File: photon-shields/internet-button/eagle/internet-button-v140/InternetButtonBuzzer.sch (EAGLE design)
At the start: 41 parts

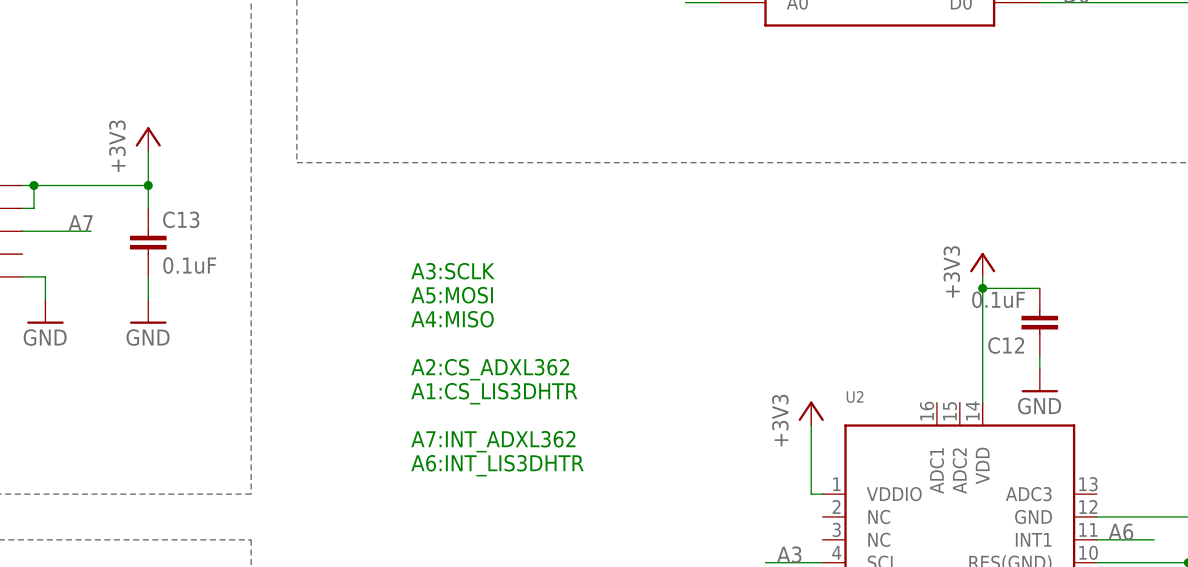
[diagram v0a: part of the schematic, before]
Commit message: update the arrow for silkscreen
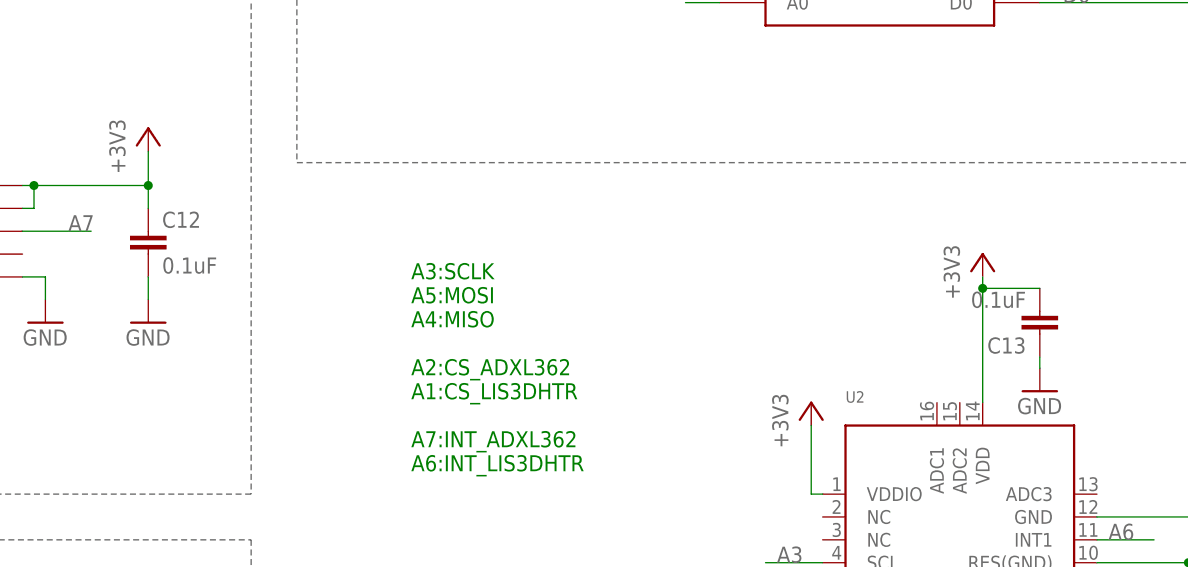
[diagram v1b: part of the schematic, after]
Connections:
- net +3V3: now also C12.1, C13.2; no longer C12.2, C13.1
- net GND: now also C12.2, C13.1; no longer C12.1, C13.2
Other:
- moved on the sheet: C12, C13
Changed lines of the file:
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@@
 <?xml version="1.0" encoding="utf-8"?>
 <!DOCTYPE eagle SYSTEM "eagle.dtd">
-<eagle version="7.7.0">
+<eagle version="8.2.2">
 <drawing>
 <settings>
@@
 <part name="R1" library="SparkFun-Resistors" deviceset="470OHM1/10W1%(0603)" device="" value="470"/>
 <part name="U1" library="SparkFun-Sensors" deviceset="ADXL362" device="ADXL362-1:1"/>
-<part name="C13" library="SparkFun-Passives" deviceset="CAP" device="0603-CAP" value="0.1uF"/>
+<part name="C12" library="SparkFun-Passives" deviceset="CAP" device="0603-CAP" value="0.1uF"/>
 <part name="GND3" library="SparkFun-Aesthetics" deviceset="GND" device=""/>
 <part name="U$2" library="Spark" deviceset="12MM_TACTILE_SWITCH" device=""/>
@@
 <part name="+3V1" library="supply1" deviceset="+3V3" device=""/>
 <part name="+3V5" library="supply1" deviceset="+3V3" device=""/>
-<part name="C12" library="SparkFun-Passives" deviceset="CAP" device="0603-CAP" value="0.1uF"/>
+<part name="C13" library="SparkFun-Passives" deviceset="CAP" device="0603-CAP" value="0.1uF"/>
 <part name="R2" library="SparkFun-Resistors" deviceset="470OHM1/10W1%(0603)" device="" value="10K"/>
 <part name="+3V6" library="supply1" deviceset="+3V3" device=""/>
@@
 <instance part="R1" gate="G$1" x="82.55" y="247.65"/>
 <instance part="U1" gate="G$1" x="129.54" y="125.73"/>
-<instance part="C13" gate="G$1" x="158.75" y="123.19"/>
+<instance part="C12" gate="G$1" x="158.75" y="123.19"/>
 <instance part="GND3" gate="1" x="158.75" y="115.57"/>
 <instance part="U$2" gate="G$1" x="135.89" y="73.66" smashed="yes">
@@
 <instance part="+3V1" gate="G$1" x="232.41" y="106.68"/>
 <instance part="+3V5" gate="G$1" x="251.46" y="123.19"/>
-<instance part="C12" gate="G$1" x="257.81" y="116.84" rot="R180"/>
+<instance part="C13" gate="G$1" x="257.81" y="116.84" rot="R180"/>
 <instance part="R2" gate="G$1" x="267.97" y="73.66" rot="R90"/>
 <instance part="+3V6" gate="G$1" x="267.97" y="82.55"/>
@@
 </segment>
 <segment>
-<pinref part="C13" gate="G$1" pin="2"/>
+<pinref part="C12" gate="G$1" pin="2"/>
 <pinref part="GND3" gate="1" pin="GND"/>
 <wire x1="158.75" y1="120.65" x2="158.75" y2="118.11" width="0.1524" layer="91"/>
@@
 </segment>
 <segment>
-<pinref part="C12" gate="G$1" pin="1"/>
+<pinref part="C13" gate="G$1" pin="1"/>
 <pinref part="GND22" gate="1" pin="GND"/>
 <wire x1="257.81" y1="111.76" x2="257.81" y2="110.49" width="0.1524" layer="91"/>
@@
 <pinref part="U2" gate="G$1" pin="VDD"/>
 <wire x1="251.46" y1="120.65" x2="251.46" y2="119.38" width="0.1524" layer="91"/>
-<pinref part="C12" gate="G$1" pin="2"/>
+<pinref part="C13" gate="G$1" pin="2"/>
 <wire x1="251.46" y1="119.38" x2="251.46" y2="106.68" width="0.1524" layer="91"/>
 <wire x1="257.81" y1="119.38" x2="251.46" y2="119.38" width="0.1524" layer="91"/>
@@
 <pinref part="U1" gate="G$1" pin="VDDIO"/>
 <wire x1="144.78" y1="130.81" x2="146.05" y2="130.81" width="0.1524" layer="91"/>
-<pinref part="C13" gate="G$1" pin="1"/>
+<pinref part="C12" gate="G$1" pin="1"/>
 <wire x1="158.75" y1="128.27" x2="158.75" y2="130.81" width="0.1524" layer="91"/>
 <wire x1="158.75" y1="130.81" x2="146.05" y2="130.81" width="0.1524" layer="91"/>
